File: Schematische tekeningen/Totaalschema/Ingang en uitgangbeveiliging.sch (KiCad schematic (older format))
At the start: 25 parts

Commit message: Footprints toegevoegd en toegewezen. Tekening weer iets aangepast
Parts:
- C2, C3: footprint (none) -> Capacitor_SMD:C_0603_1608Metric_Pad1.08x0.95mm_HandSolder
- C7, C8: renamed from C?; footprint (none) -> Capacitor_SMD:C_0603_1608Metric_Pad1.08x0.95mm_HandSolder
- IC2: renamed from IC?; footprint SOIC127P1150X280-8N -> eec:SOIC127P1150X280-8N
- R10, R11, R12, R13, R14, R15, R16, R17, R18, R5, R6, R7, R8, R9: renamed from R?; footprint (none) -> Resistor_SMD:R_0603_1608Metric_Pad0.98x0.95mm_HandSolder
- U2: renamed from U?; footprint 21-0041_S16+1_MXM -> eec:MAX14933ASE&plus_T
- gave numbers to parts that had none: 5
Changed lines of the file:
@@
 P 925 1375
 AR Path="/61891674" Ref="C2"  Part="1"
-AR Path="/618861AB/61891674" Ref="C?"  Part="1"
-F 0 "C?" V 875 1475 50  0000 C CNN
+AR Path="/618861AB/61891674" Ref="C5"  Part="1"
+F 0 "C5" V 875 1475 50  0000 C CNN
 F 1 "100n" V 800 1400 50  0000 C CNN
-F 2 "" H 925 1375 50  0001 C CNN
+F 2 "Capacitor_SMD:C_0603_1608Metric_Pad1.08x0.95mm_HandSolder" H 925 1375 50  0001 C CNN
 F 3 "~" H 925 1375 50  0001 C CNN
 	1    925  1375
@@
 	1025 1425 1325 1425
 $Comp
-L 2021-11-20_15-23-40:MAX14933ASE+T U?
+L 2021-11-20_15-23-40:MAX14933ASE+T U2
 U 1 1 619B095B
 P 1325 1225
-F 0 "U?" H 2225 1612 60  0000 C CNN
+F 0 "U2" H 2225 1612 60  0000 C CNN
 F 1 "MAX14933ASE+T" H 2225 1506 60  0000 C CNN
-F 2 "21-0041_S16+1_MXM" H 2225 1465 60  0001 C CNN
+F 2 "eec:MAX14933ASE&plus_T" H 2225 1465 60  0001 C CNN
 F 3 "" H 1325 1225 60  0000 C CNN
 	1    1325 1225
@@
 UART Isolatie
 $Comp
-L Device:R_Small R?
+L Device:R_Small R12
 U 1 1 619A7D62
 P 3275 1675
-F 0 "R?" V 3200 1700 39  0000 C CNN
+F 0 "R12" V 3200 1700 39  0000 C CNN
 F 1 "10k" V 3275 1675 39  0000 C CNN
-F 2 "" H 3275 1675 50  0001 C CNN
+F 2 "Resistor_SMD:R_0603_1608Metric_Pad0.98x0.95mm_HandSolder" H 3275 1675 50  0001 C CNN
 F 3 "~" H 3275 1675 50  0001 C CNN
 	1    3275 1675
@@
 $EndComp
 $Comp
-L Device:R_Small R?
+L Device:R_Small R13
 U 1 1 619A9AB5
 P 3300 1800
-F 0 "R?" V 3350 1800 39  0000 C CNN
+F 0 "R13" V 3350 1800 39  0000 C CNN
 F 1 "10k" V 3300 1800 39  0000 C CNN
-F 2 "" H 3300 1800 50  0001 C CNN
+F 2 "Resistor_SMD:R_0603_1608Metric_Pad0.98x0.95mm_HandSolder" H 3300 1800 50  0001 C CNN
 F 3 "~" H 3300 1800 50  0001 C CNN
 	1    3300 1800
@@
 P 3400 1400
 AR Path="/61891659" Ref="C3"  Part="1"
-AR Path="/618861AB/61891659" Ref="C?"  Part="1"
-F 0 "C?" H 3525 1400 50  0000 C CNN
+AR Path="/618861AB/61891659" Ref="C6"  Part="1"
+F 0 "C6" H 3525 1400 50  0000 C CNN
 F 1 "100n" H 3225 1400 50  0000 C CNN
-F 2 "" H 3400 1400 50  0001 C CNN
+F 2 "Capacitor_SMD:C_0603_1608Metric_Pad1.08x0.95mm_HandSolder" H 3400 1400 50  0001 C CNN
 F 3 "~" H 3400 1400 50  0001 C CNN
 	1    3400 1400
@@
 	3200 1425 3125 1425
 $Comp
-L Device:R_Small R?
+L Device:R_Small R6
 U 1 1 619D40A3
 P 1175 1550
-F 0 "R?" V 1225 1650 39  0000 C CNN
+F 0 "R6" V 1225 1650 39  0000 C CNN
 F 1 "10k" V 1175 1550 39  0000 C CNN
-F 2 "" H 1175 1550 50  0001 C CNN
+F 2 "Resistor_SMD:R_0603_1608Metric_Pad0.98x0.95mm_HandSolder" H 1175 1550 50  0001 C CNN
 F 3 "~" H 1175 1550 50  0001 C CNN
 	1    1175 1550
@@
 $EndComp
 $Comp
-L Device:R_Small R?
+L Device:R_Small R7
 U 1 1 619D46F5
 P 1175 1675
-F 0 "R?" V 1200 1775 39  0000 C CNN
+F 0 "R7" V 1200 1775 39  0000 C CNN
 F 1 "10k" V 1175 1675 39  0000 C CNN
-F 2 "" H 1175 1675 50  0001 C CNN
+F 2 "Resistor_SMD:R_0603_1608Metric_Pad0.98x0.95mm_HandSolder" H 1175 1675 50  0001 C CNN
 F 3 "~" H 1175 1675 50  0001 C CNN
 	1    1175 1675
@@
 	1050 1550 1075 1550
 $Comp
-L ISO6721QDWVRQ1:ISO6721QDWVRQ1 IC?
+L ISO6721QDWVRQ1:ISO6721QDWVRQ1 IC2
 U 1 1 619DF44C
 P 5650 1325
-F 0 "IC?" H 6200 1590 50  0000 C CNN
+F 0 "IC2" H 6200 1590 50  0000 C CNN
 F 1 "ISO6721QDWVRQ1" H 6200 1499 50  0000 C CNN
-F 2 "SOIC127P1150X280-8N" H 6600 1425 50  0001 L CNN
+F 2 "eec:SOIC127P1150X280-8N" H 6600 1425 50  0001 L CNN
 F 3 "https://www.ti.com/lit/gpn/iso6721-q1" H 6600 1325 50  0001 L CNN
 F 4 "Digital Isolators Automotive, general-purpose, dual-channel, 1/1 digital isolator" H 6600 1225 50  0001 L CNN "Description"
@@
 P 7175 1225
 AR Path="/619E2D2F" Ref="C?"  Part="1"
-AR Path="/618861AB/619E2D2F" Ref="C?"  Part="1"
-F 0 "C?" H 7300 1225 50  0000 C CNN
+AR Path="/618861AB/619E2D2F" Ref="C8"  Part="1"
+F 0 "C8" H 7300 1225 50  0000 C CNN
 F 1 "100n" H 7000 1225 50  0000 C CNN
-F 2 "" H 7175 1225 50  0001 C CNN
+F 2 "Capacitor_SMD:C_0603_1608Metric_Pad1.08x0.95mm_HandSolder" H 7175 1225 50  0001 C CNN
 F 3 "~" H 7175 1225 50  0001 C CNN
 	1    7175 1225
@@
 P 5250 1275
 AR Path="/619E5AEE" Ref="C?"  Part="1"
-AR Path="/618861AB/619E5AEE" Ref="C?"  Part="1"
-F 0 "C?" V 5200 1375 50  0000 C CNN
+AR Path="/618861AB/619E5AEE" Ref="C7"  Part="1"
+F 0 "C7" V 5200 1375 50  0000 C CNN
 F 1 "100n" V 5125 1300 50  0000 C CNN
-F 2 "" H 5250 1275 50  0001 C CNN
+F 2 "Capacitor_SMD:C_0603_1608Metric_Pad1.08x0.95mm_HandSolder" H 5250 1275 50  0001 C CNN
 F 3 "~" H 5250 1275 50  0001 C CNN
 	1    5250 1275
@@
 TTL Isolatie (Verzendkant)
 $Comp
-L Isolator:PC817 U?
+L Isolator:PC817 U6
 U 1 1 619FB6E2
 P 9775 1425
-F 0 "U?" H 9775 1750 50  0000 C CNN
+F 0 "U6" H 9775 1750 50  0000 C CNN
 F 1 "PC817" H 9775 1659 50  0000 C CNN
 F 2 "Package_DIP:DIP-4_W7.62mm" H 9575 1225 50  0001 L CIN
@@
 TTL Isolatie (Ontvangkant)
 $Comp
-L Isolator:PC817 U?
+L Isolator:PC817 U5
 U 1 1 61A04A84
 P 2925 3650
-F 0 "U?" H 2925 3975 50  0000 C CNN
+F 0 "U5" H 2925 3975 50  0000 C CNN
 F 1 "PC817" H 2925 3884 50  0000 C CNN
 F 2 "Package_DIP:DIP-4_W7.62mm" H 2725 3450 50  0001 L CIN
@@
 $EndComp
 $Comp
-L Device:R_Small R?
+L Device:R_Small R14
 U 1 1 61A0AE0B
 P 3325 3550
-F 0 "R?" V 3521 3550 50  0000 C CNN
+F 0 "R14" V 3521 3550 50  0000 C CNN
 F 1 "1k" V 3430 3550 50  0000 C CNN
-F 2 "" H 3325 3550 50  0001 C CNN
+F 2 "Resistor_SMD:R_0603_1608Metric_Pad0.98x0.95mm_HandSolder" H 3325 3550 50  0001 C CNN
 F 3 "~" H 3325 3550 50  0001 C CNN
 	1    3325 3550
@@
 $EndComp
 $Comp
-L Device:R_Small R?
+L Device:R_Small R11
 U 1 1 61A0D471
 P 2625 3450
-F 0 "R?" H 2567 3404 50  0000 R CNN
+F 0 "R11" H 2567 3404 50  0000 R CNN
 F 1 "1k" H 2567 3495 50  0000 R CNN
-F 2 "" H 2625 3450 50  0001 C CNN
+F 2 "Resistor_SMD:R_0603_1608Metric_Pad0.98x0.95mm_HandSolder" H 2625 3450 50  0001 C CNN
 F 3 "~" H 2625 3450 50  0001 C CNN
 	1    2625 3450
@@
 VCC
 $Comp
-L Isolator:PC817 U?
+L Isolator:PC817 U3
 U 1 1 61A14519
 P 1450 3250
-F 0 "U?" H 1450 3575 50  0000 C CNN
+F 0 "U3" H 1450 3575 50  0000 C CNN
 F 1 "PC817" H 1450 3484 50  0000 C CNN
 F 2 "Package_DIP:DIP-4_W7.62mm" H 1250 3050 50  0001 L CIN
@@
 $EndComp
 $Comp
-L Device:R_Small R?
+L Device:R_Small R9
 U 1 1 61A1451F
 P 1850 3150
-F 0 "R?" V 2046 3150 50  0000 C CNN
+F 0 "R9" V 2046 3150 50  0000 C CNN
 F 1 "1k" V 1955 3150 50  0000 C CNN
-F 2 "" H 1850 3150 50  0001 C CNN
+F 2 "Resistor_SMD:R_0603_1608Metric_Pad0.98x0.95mm_HandSolder" H 1850 3150 50  0001 C CNN
 F 3 "~" H 1850 3150 50  0001 C CNN
 	1    1850 3150
@@
 $EndComp
 $Comp
-L Device:R_Small R?
+L Device:R_Small R5
 U 1 1 61A14525
 P 1150 3050
-F 0 "R?" H 1092 3004 50  0000 R CNN
+F 0 "R5" H 1092 3004 50  0000 R CNN
 F 1 "1k" H 1092 3095 50  0000 R CNN
-F 2 "" H 1150 3050 50  0001 C CNN
+F 2 "Resistor_SMD:R_0603_1608Metric_Pad0.98x0.95mm_HandSolder" H 1150 3050 50  0001 C CNN
 F 3 "~" H 1150 3050 50  0001 C CNN
 	1    1150 3050
@@
 VCC
 $Comp
-L Isolator:PC817 U?
+L Isolator:PC817 U4
 U 1 1 61A1553A
 P 1575 4075
-F 0 "U?" H 1575 4400 50  0000 C CNN
+F 0 "U4" H 1575 4400 50  0000 C CNN
 F 1 "PC817" H 1575 4309 50  0000 C CNN
 F 2 "Package_DIP:DIP-4_W7.62mm" H 1375 3875 50  0001 L CIN
@@
 $EndComp
 $Comp
-L Device:R_Small R?
+L Device:R_Small R10
 U 1 1 61A15540
 P 1975 3975
-F 0 "R?" V 2171 3975 50  0000 C CNN
+F 0 "R10" V 2171 3975 50  0000 C CNN
 F 1 "1k" V 2080 3975 50  0000 C CNN
-F 2 "" H 1975 3975 50  0001 C CNN
+F 2 "Resistor_SMD:R_0603_1608Metric_Pad0.98x0.95mm_HandSolder" H 1975 3975 50  0001 C CNN
 F 3 "~" H 1975 3975 50  0001 C CNN
 	1    1975 3975
@@
 $EndComp
 $Comp
-L Device:R_Small R?
+L Device:R_Small R8
 U 1 1 61A15546
 P 1275 3875
-F 0 "R?" H 1217 3829 50  0000 R CNN
+F 0 "R8" H 1217 3829 50  0000 R CNN
 F 1 "1k" H 1217 3920 50  0000 R CNN
-F 2 "" H 1275 3875 50  0001 C CNN
+F 2 "Resistor_SMD:R_0603_1608Metric_Pad0.98x0.95mm_HandSolder" H 1275 3875 50  0001 C CNN
 F 3 "~" H 1275 3875 50  0001 C CNN
 	1    1275 3875
@@
 Status_MCU
 $Comp
-L Device:R_Small R?
+L Device:R_Small R15
 U 1 1 61A4AED4
 P 9375 1325
-F 0 "R?" V 9571 1325 50  0000 C CNN
+F 0 "R15" V 9571 1325 50  0000 C CNN
 F 1 "1k" V 9480 1325 50  0000 C CNN
-F 2 "" H 9375 1325 50  0001 C CNN
+F 2 "Resistor_SMD:R_0603_1608Metric_Pad0.98x0.95mm_HandSolder" H 9375 1325 50  0001 C CNN
 F 3 "~" H 9375 1325 50  0001 C CNN
 	1    9375 1325
@@
 VSS
 $Comp
-L Device:R_Small R?
+L Device:R_Small R17
 U 1 1 61A4CE30
 P 10075 1225
-F 0 "R?" H 10134 1271 50  0000 L CNN
+F 0 "R17" H 10134 1271 50  0000 L CNN
 F 1 "1k" H 10134 1180 50  0000 L CNN
-F 2 "" H 10075 1225 50  0001 C CNN
+F 2 "Resistor_SMD:R_0603_1608Metric_Pad0.98x0.95mm_HandSolder" H 10075 1225 50  0001 C CNN
 F 3 "~" H 10075 1225 50  0001 C CNN
 	1    10075 1225
@@
 Status_aandrijving_ISO_M
 $Comp
-L Isolator:PC817 U?
+L Isolator:PC817 U7
 U 1 1 61A518F7
 P 9775 2025
-F 0 "U?" H 9775 2350 50  0000 C CNN
+F 0 "U7" H 9775 2350 50  0000 C CNN
 F 1 "PC817" H 9775 2259 50  0000 C CNN
 F 2 "Package_DIP:DIP-4_W7.62mm" H 9575 1825 50  0001 L CIN
@@
 $EndComp
 $Comp
-L Device:R_Small R?
+L Device:R_Small R16
 U 1 1 61A518FD
 P 9375 1925
-F 0 "R?" V 9571 1925 50  0000 C CNN
+F 0 "R16" V 9571 1925 50  0000 C CNN
 F 1 "1k" V 9480 1925 50  0000 C CNN
-F 2 "" H 9375 1925 50  0001 C CNN
+F 2 "Resistor_SMD:R_0603_1608Metric_Pad0.98x0.95mm_HandSolder" H 9375 1925 50  0001 C CNN
 F 3 "~" H 9375 1925 50  0001 C CNN
 	1    9375 1925
@@
 VSS
 $Comp
-L Device:R_Small R?
+L Device:R_Small R18
 U 1 1 61A51905
 P 10075 1825
-F 0 "R?" H 10134 1871 50  0000 L CNN
+F 0 "R18" H 10134 1871 50  0000 L CNN
 F 1 "1k" H 10134 1780 50  0000 L CNN
-F 2 "" H 10075 1825 50  0001 C CNN
+F 2 "Resistor_SMD:R_0603_1608Metric_Pad0.98x0.95mm_HandSolder" H 10075 1825 50  0001 C CNN
 F 3 "~" H 10075 1825 50  0001 C CNN
 	1    10075 1825

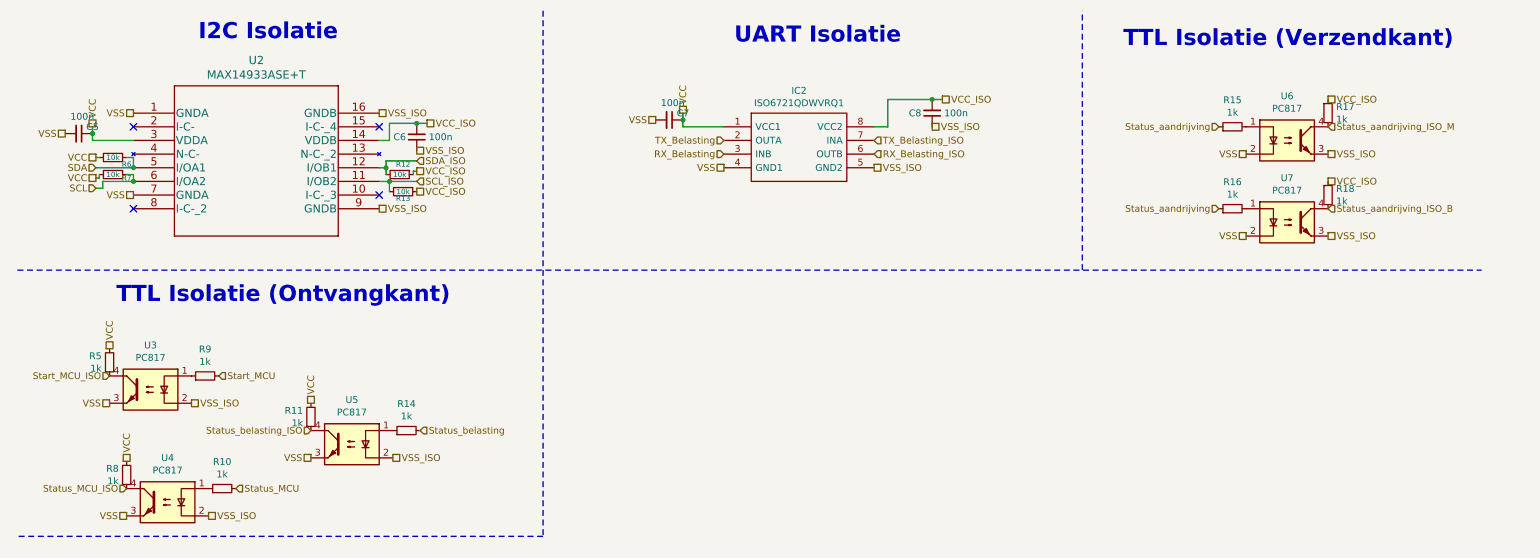
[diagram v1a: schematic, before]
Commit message: Footprints aangepast. Tekening aangepast
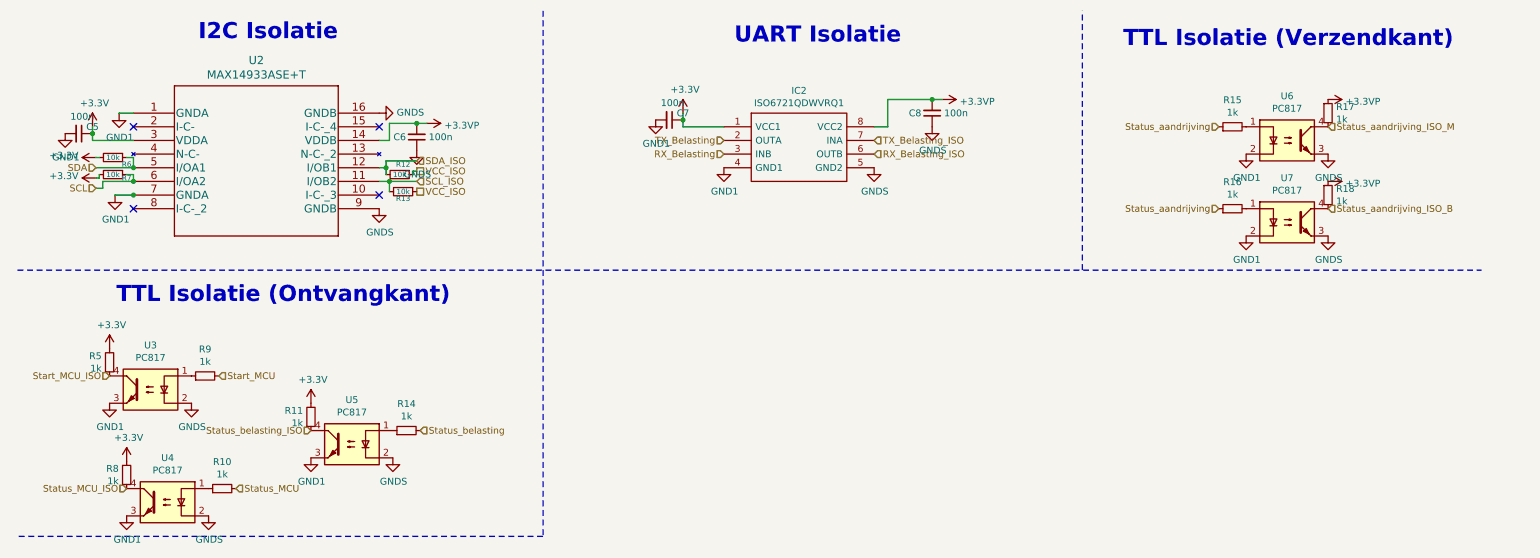
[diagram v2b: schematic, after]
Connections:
- net VCC_ISO: no longer C3.2, C8.2, IC2.8 (VCC2), R17.1, R18.1, U2.14 (VDDB)
- net VCC renamed +3V3
- net VSS renamed GND1
- net VSS_ISO renamed GNDS
- new net +3.3VP: C3.2, C8.2, IC2.8 (VCC2), R17.1, R18.1, U2.14 (VDDB)
